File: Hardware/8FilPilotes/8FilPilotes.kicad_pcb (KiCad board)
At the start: 2 copper layers, 45 x 40 mm, 11 parts, among them J1 Conn_01x04_Male, J2 Conn_02x03_Odd_Even, P1 5VIN, SW1 SW_DPST, SW2 SW_DPST, U1 AMS1117, U2 ESP-12F

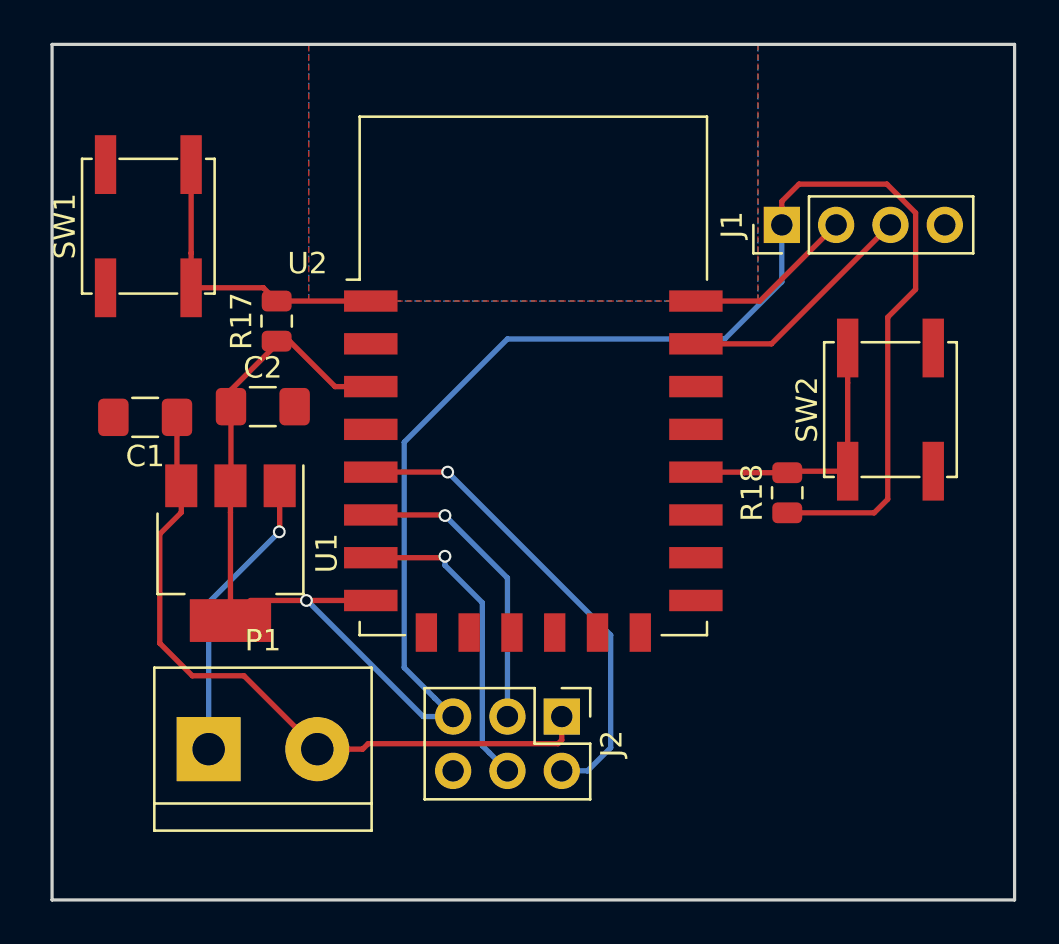
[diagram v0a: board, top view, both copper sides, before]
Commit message: - Modified almost all hardware boards : They were missing a pull-up resistor on GPIO2, which made impossible to flash. - Updated baseBoard.* files
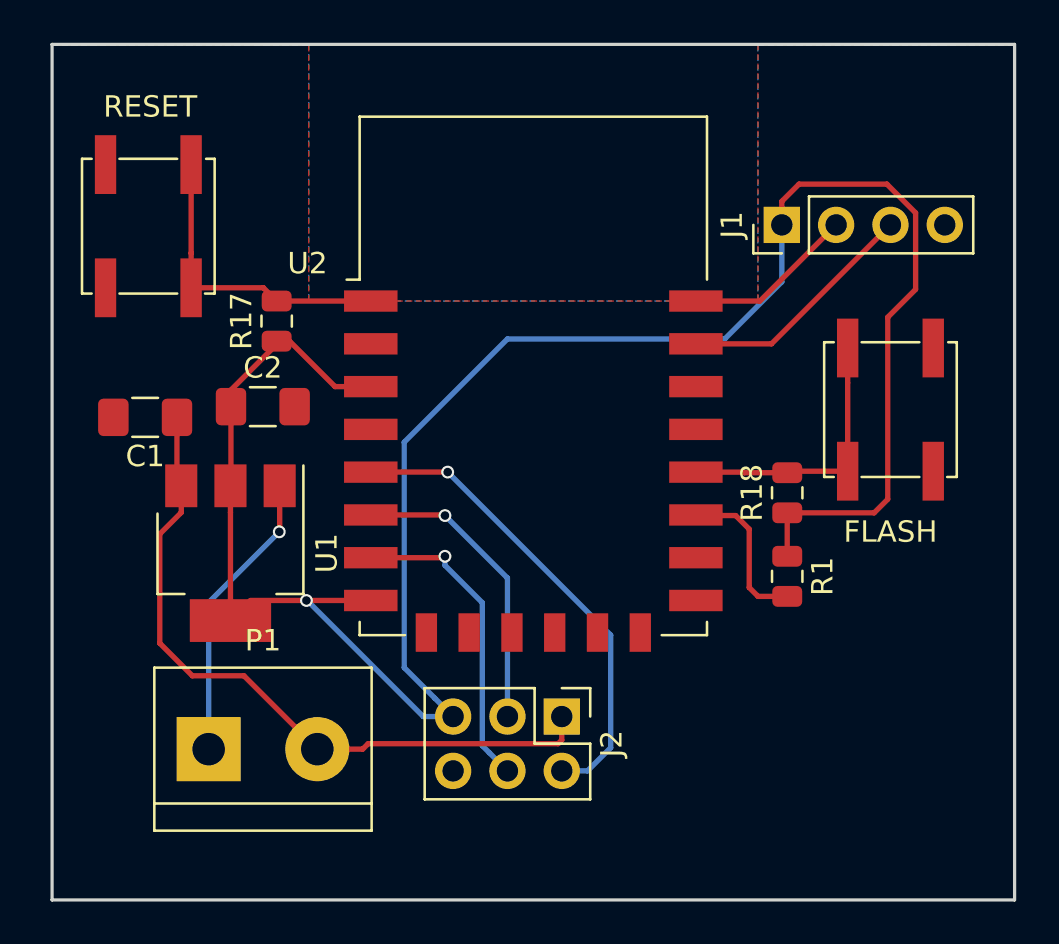
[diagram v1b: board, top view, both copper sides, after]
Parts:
- added R1: 10k, Resistor_SMD:R_0805_2012Metric, F.Cu at (174.4, 99.9)
- renumbered SW2 to FLASH, SW1 to RESET
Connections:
- U2 pad 17: (no net) -> Net-(R1-Pad2)
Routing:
- net Net-(R1-Pad2): track 0.00 -> 7.45 mm
- net /3V3: track 99.6 -> 101.7 mm
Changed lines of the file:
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@@
     (thickness 1.6)
     (drawings 5)
-    (tracks 87)
+    (tracks 95)
     (zones 0)
-    (modules 11)
-    (nets 11)
+    (modules 12)
+    (nets 12)
   )
   (page A4)
@@
   (net 9 /GND)
   (net 10 /3V3)
+  (net 11 "Net-(R1-Pad2)")
   (net_class Default "This is the default net class."
     (clearance 0.2)
@@
     (add_net /SRCLK)
     (add_net /TXD)
+    (add_net "Net-(R1-Pad2)")
     (add_net "Net-(R17-Pad2)")
     (add_net "Net-(R18-Pad2)")
@@
     (descr "Light Touch Switch")
     (attr smd)
-    (fp_text reference SW1 (at 0 -3.9 90) (layer F.SilkS)
+    (fp_text reference RESET (at 5.5855 0.0895 180) (layer F.SilkS)
       (effects (font (size 1 1) (thickness 0.15)))
     )
@@
     (descr "Light Touch Switch")
     (attr smd)
-    (fp_text reference SW2 (at 0 -3.9 90) (layer F.SilkS)
+    (fp_text reference FLASH (at -5.715 0 180) (layer F.SilkS)
       (effects (font (size 1 1) (thickness 0.15)))
     )
@@
     (pad 16 smd rect (at 7.6 8.5) (size 2.5 1) (layers F.Cu F.Paste F.Mask)
       (net 9 /GND))
-    (pad 17 smd rect (at 7.6 6.5) (size 2.5 1) (layers F.Cu F.Paste F.Mask))
+    (pad 17 smd rect (at 7.6 6.5) (size 2.5 1) (layers F.Cu F.Paste F.Mask)
+      (net 11 "Net-(R1-Pad2)"))
     (pad 18 smd rect (at 7.6 4.5) (size 2.5 1) (layers F.Cu F.Paste F.Mask)
       (net 7 "Net-(R18-Pad2)"))
@@
       (net 4 /TXD))
     (model ${KISYS3DMOD}/RF_Module.3dshapes/ESP-12E.wrl
+      (at (xyz 0 0 0))
+      (scale (xyz 1 1 1))
+      (rotate (xyz 0 0 0))
+    )
+  )
+  (module Resistor_SMD:R_0805_2012Metric (layer F.Cu)
+    (at 174.371 99.8705 270)
+    (descr "Resistor SMD 0805 (2012 Metric), square (rectangular) end terminal, IPC_7351 nominal, (Body size source: https://docs.google.com/spreadsheets/d/1BsfQQcO9C6DZCsRaXUlFlo91Tg2WpOkGARC1WS5S8t0/edit?usp=sharing), generated with kicad-footprint-generator")
+    (tags resistor)
+    (attr smd)
+    (fp_text reference R1 (at 0 -1.65 270) (layer F.SilkS)
+      (effects (font (size 1 1) (thickness 0.15)))
+    )
+    (fp_text value 10k (at 0 1.65 270) (layer F.Fab)
+      (effects (font (size 1 1) (thickness 0.15)))
+    )
+    (fp_line (start -1 0.6) (end -1 -0.6) (layer F.Fab) (width 0.1))
+    (fp_line (start -1 -0.6) (end 1 -0.6) (layer F.Fab) (width 0.1))
+    (fp_line (start 1 -0.6) (end 1 0.6) (layer F.Fab) (width 0.1))
+    (fp_line (start 1 0.6) (end -1 0.6) (layer F.Fab) (width 0.1))
+    (fp_line (start -0.258578 -0.71) (end 0.258578 -0.71) (layer F.SilkS) (width 0.12))
+    (fp_line (start -0.258578 0.71) (end 0.258578 0.71) (layer F.SilkS) (width 0.12))
+    (fp_line (start -1.68 0.95) (end -1.68 -0.95) (layer F.CrtYd) (width 0.05))
+    (fp_line (start -1.68 -0.95) (end 1.68 -0.95) (layer F.CrtYd) (width 0.05))
+    (fp_line (start 1.68 -0.95) (end 1.68 0.95) (layer F.CrtYd) (width 0.05))
+    (fp_line (start 1.68 0.95) (end -1.68 0.95) (layer F.CrtYd) (width 0.05))
+    (fp_text user %R (at 0 0 270) (layer F.Fab)
+      (effects (font (size 0.5 0.5) (thickness 0.08)))
+    )
+    (pad 1 smd roundrect (at -0.9375 0 270) (size 0.975 1.4) (layers F.Cu F.Paste F.Mask) (roundrect_rratio 0.25)
+      (net 10 /3V3))
+    (pad 2 smd roundrect (at 0.9375 0 270) (size 0.975 1.4) (layers F.Cu F.Paste F.Mask) (roundrect_rratio 0.25)
+      (net 11 "Net-(R1-Pad2)"))
+    (model ${KISYS3DMOD}/Resistor_SMD.3dshapes/R_0805_2012Metric.wrl
       (at (xyz 0 0 0))
       (scale (xyz 1 1 1))
@@
   (segment (start 156.464 93.599) (end 156.464 104.14) (width 0.25) (layer B.Cu) (net 10))
   (segment (start 156.464 104.14) (end 157.900001 105.576001) (width 0.25) (layer B.Cu) (net 10))
+  (segment (start 174.371 98.933) (end 174.371 96.901) (width 0.25) (layer F.Cu) (net 10))
+  (segment (start 170.1 97) (end 170.85 97) (width 0.25) (layer F.Cu) (net 11))
+  (segment (start 171.958 97.028) (end 172.593 97.663) (width 0.25) (layer F.Cu) (net 11))
+  (segment (start 170.878 97.028) (end 171.958 97.028) (width 0.25) (layer F.Cu) (net 11))
+  (segment (start 173.0075 100.808) (end 174.371 100.808) (width 0.25) (layer F.Cu) (net 11))
+  (segment (start 170.85 97) (end 170.878 97.028) (width 0.25) (layer F.Cu) (net 11))
+  (segment (start 172.593 97.663) (end 172.593 100.3935) (width 0.25) (layer F.Cu) (net 11))
+  (segment (start 172.593 100.3935) (end 173.0075 100.808) (width 0.25) (layer F.Cu) (net 11))
   (zone (net 9) (net_name /GND) (layer F.Cu) (hatch edge 0.508)
     (connect_pads (clearance 0.508))
